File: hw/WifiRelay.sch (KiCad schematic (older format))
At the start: 34 parts, among them J1 CONN_01X02, J2 CONN_01X06, J3 CONN_01X02, J4 CONN_01X02, J5 TEST_1P, K1 Songle-SRD-05VDC-SL-C, K2 Songle-SRD-05VDC-SL-C, Q1 MMSS8050-H, Q2 MMSS8050-H, SW1 SW_Push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

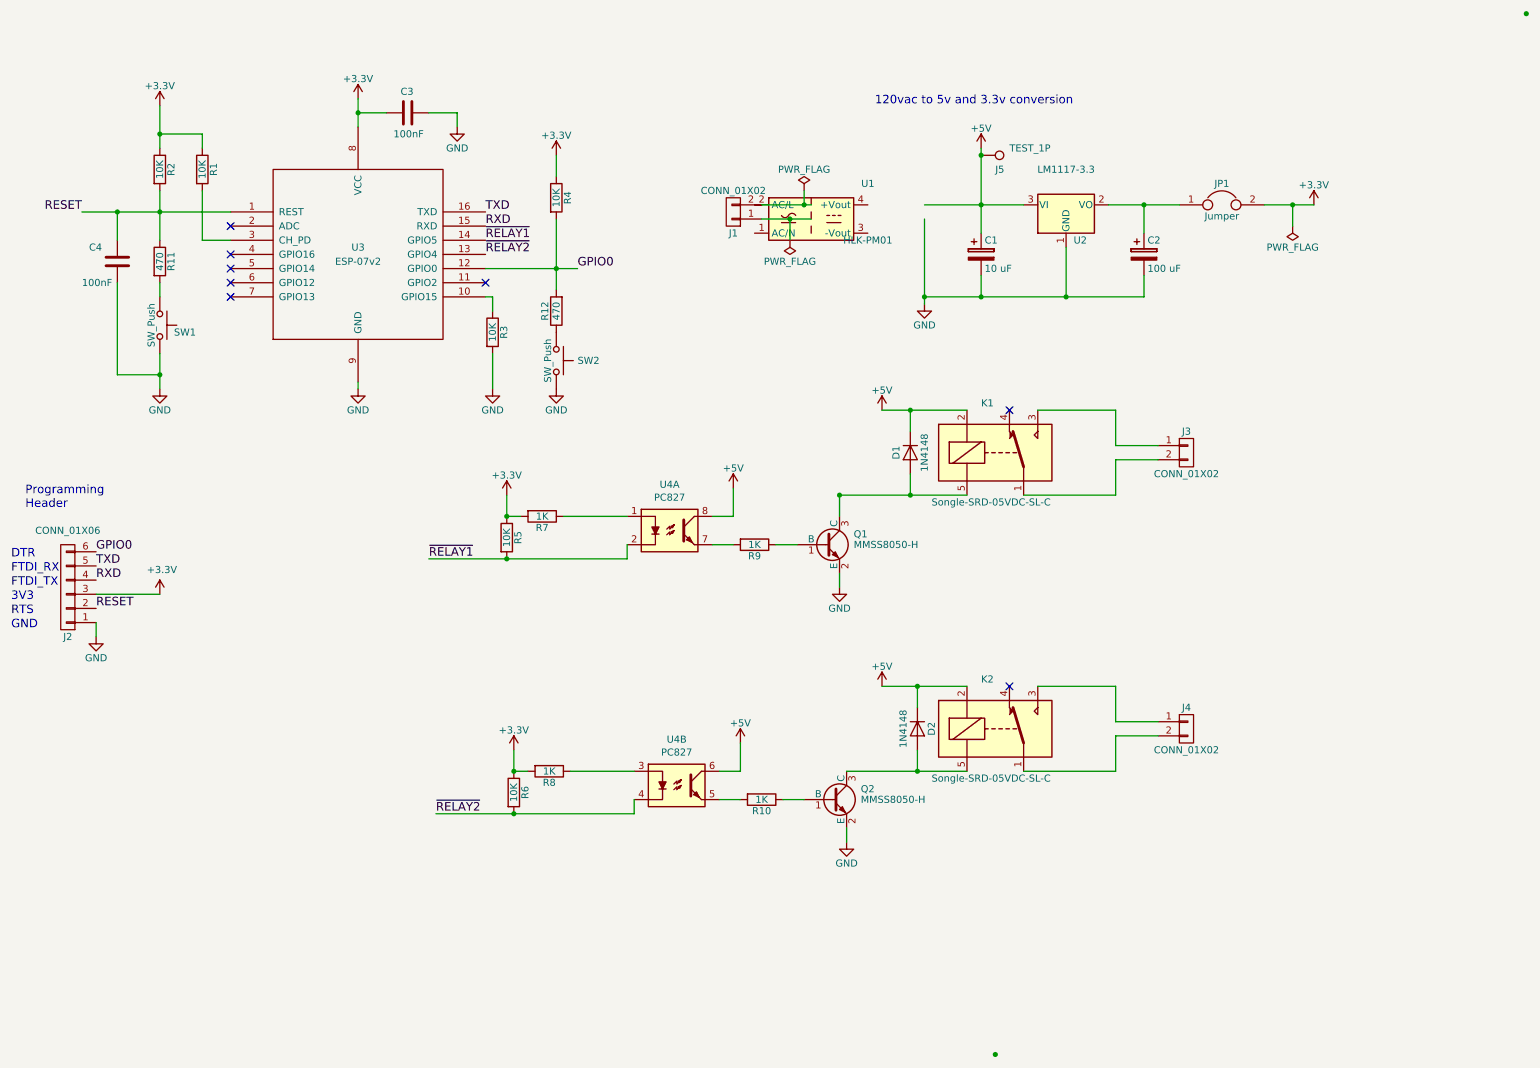
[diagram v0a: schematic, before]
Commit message: Silkscreen updates to programming header, changed 3.3v power jumper to two positions
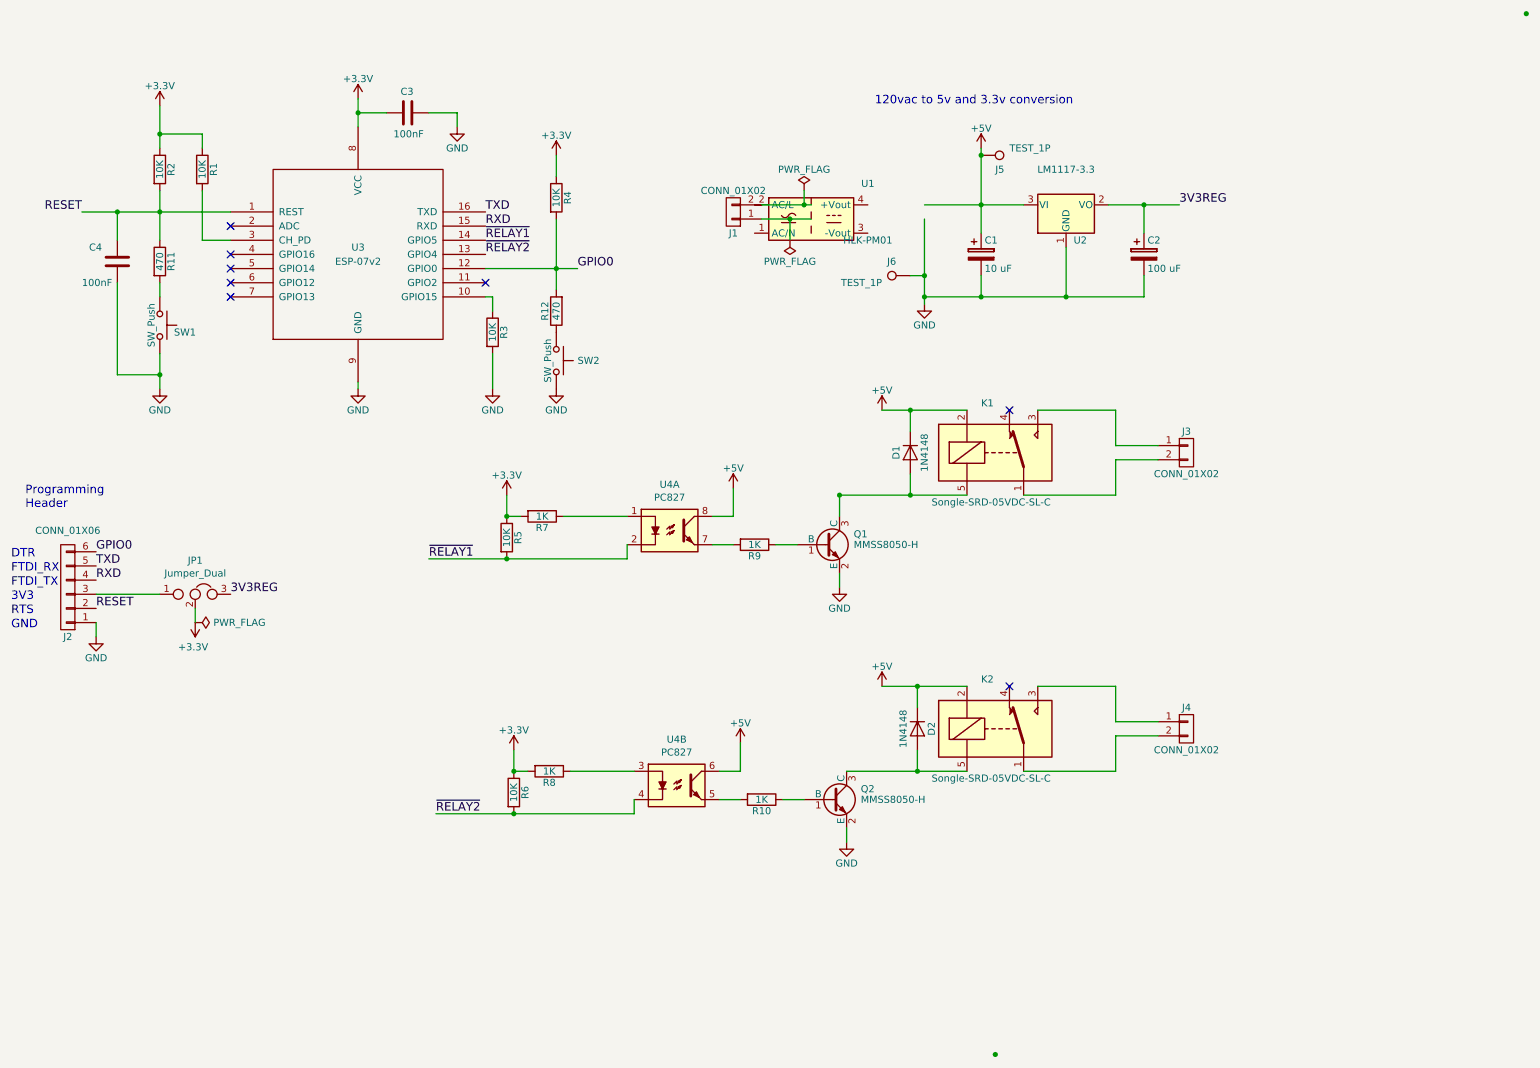
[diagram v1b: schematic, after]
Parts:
- removed JP1: Jumper, Pin_Headers:Pin_Header_Straight_1x02_Pitch2.54mm, symbol Jumper
- added J6: TEST_1P, Pin_Headers:Pin_Header_Straight_1x01_Pitch2.54mm, symbol TEST_1P
- added JP1: Jumper_Dual, Pin_Headers:Pin_Header_Straight_1x03_Pitch2.54mm, symbol Jumper_Dual
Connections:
- net labels added: 3V3REG

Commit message: Update for consistency with KiCad 5.02
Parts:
- removed D1, D2: 1N4148, Diodes_SMD:D_SOD-123, symbol 1N4148
- removed J1, J3, J4: CONN_01X02, Connectors_Terminal_Blocks:TerminalBlock_Pheonix_MKDS1.5-2pol, symbol CONN_01X02
- removed J2: CONN_01X06, Pin_Headers:Pin_Header_Straight_1x06_Pitch2.54mm, symbol CONN_01X06
- removed JP1: Jumper_Dual, Pin_Headers:Pin_Header_Straight_1x03_Pitch2.54mm, symbol Jumper_Dual
- removed K1, K2: Songle-SRD-05VDC-SL-C, Relays_THT:Relay_SPDT_SANYOU_SRD_Series_Form_C, symbol Songle-SRD-05VDC-SL-C
- removed U1: HLK-PM01, WifiRelay:HLK-PM01, symbol IRM-02-5
- removed U2: LM1117-3.3, TO_SOT_Packages_SMD:SOT-223-3Lead_TabPin2, symbol LM1117-3.3
- removed U4: PC827, WifiRelay:SOIC-8, symbol PC827
- added D1, D2: 1N4148W, Diode_SMD:D_SOD-123, symbol Diode:1N4148W
- added J1, J3, J4: Conn_01x02_Female, symbol Connector:Conn_01x02_Female
- added J2: Conn_01x06_Male, symbol Connector:Conn_01x06_Male
- added JP1: Jumper_3_Bridged12, symbol Jumper:Jumper_3_Bridged12
- added K1, K2: SANYOU_SRD_Form_C, Relay_THT:Relay_SPDT_SANYOU_SRD_Series_Form_C, symbol Relay:SANYOU_SRD_Form_C
- added U1: IRM-02-5, Converter_ACDC:Converter_ACDC_MeanWell_IRM-02-xx_THT, symbol Converter_ACDC:IRM-02-5
- added U2: LM1117-3.3, symbol Regulator_Linear:LM1117-3.3
- added U4: PC827, Package_DIP:DIP-8_W7.62mm, symbol Isolator:PC827
- C1, C2: symbol CP -> Device:CP
- C3, C4: symbol C -> Device:C
- J5, J6: symbol TEST_1P -> WifiRelay-rescue:TEST_1P
- Q1, Q2: symbol MMSS8050-H -> WifiRelay-rescue:MMSS8050-H
- R1, R10, R11, R12, R2, R3, R4, R5, R6, R7, R8, R9: symbol R -> Device:R
- SW1, SW2: symbol SW_Push -> WifiRelay-rescue:SW_Push
- U3: symbol ESP-07v2 -> WifiRelay-rescue:ESP-07v2
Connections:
- wire segments 82 -> 109
